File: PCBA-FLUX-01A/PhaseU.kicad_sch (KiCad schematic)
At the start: 60 parts, among them Q2 IPT015N10N5, Q3 IPT015N10N5, Q4 IPT015N10N5, Q5 IPT015N10N5, Q6 BC817, U2 INA240A2DR, U3 UCC27211AQDDARQ1, U4 TLV9001

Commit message: Changes were made
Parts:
- added C104: C, Capacitor_THT:C_Rect_L9.0mm_W6.4mm_P7.50mm_MKT, symbol Device:C
- added C95: 10nF, Capacitor_SMD:C_0603_1608Metric, symbol Device:C
- added R76, R77, R78, R79: 10R, Resistor_SMD:R_0805_2012Metric, symbol Device:R
- added R90: R, Resistor_SMD:R_1218_3246Metric, symbol Device:R
- R1, R17, R2: footprint Resistor_SMD:R_0805_2012Metric -> Resistor_SMD:R_0603_1608Metric
- R3: footprint Resistor_SMD:R_0805_2012Metric -> palmkiLib:R_0603_1608Metric
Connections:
- net GND: now also C104.2
- net phU_Shunt+: now also R76.1, R77.1; no longer U2.8 (IN+)
- net phU_Shunt-: now also R78.1, R79.1; no longer U2.1 (IN-)
- net at C37.2, C38.2, Q2.2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: now also R90.1
- new net: C95.1, R76.2, R77.2, U2.8 (IN+)
- new net: C95.2, R78.2, R79.2, U2.1 (IN-)
- new net: C104.1, R90.2
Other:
- moved on the sheet: C29, C30, C31, C32, C33, C34, C35, C36, C37, C38, D2, D3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

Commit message: Finished schematic?
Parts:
- removed C42, C44, C46, C49: 2.2uF, Capacitor_SMD:C_1210_3225Metric, symbol Device:C
- removed Q6: BC817, Package_TO_SOT_SMD:SOT-23, symbol Transistor_BJT:BC817
- removed R24: 2K2, Resistor_SMD:R_0603_1608Metric, symbol Device:R
- added C107, C108, C109, C110, C111: 1000uF, Capacitor_THT:CP_Radial_D18.0mm_P7.50mm, symbol Device:C_Polarized
- added C112, C113, C114, C115, C116: 10uF, Capacitor_SMD:C_1210_3225Metric, symbol Device:C
- added C117: 100nF, Capacitor_SMD:C_0805_2012Metric, symbol Device:C
- added Q18: BC860C, Package_TO_SOT_SMD:SOT-23, symbol Simulation_SPICE:PNP
- added R93: 18k, Resistor_SMD:R_0603_1608Metric, symbol Synapse:R
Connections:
- net +3.3VA: now also Q18.3 (E), R93.1
- net +VSYS: now also C107.1, C108.1, C109.1, C110.1, C111.1, C112.1, C113.1, C114.1, C115.1, C116.1, C117.1
- net GND: now also C107.2, C108.2, C109.2, C110.2, C111.2, C112.2, C113.2, C114.2, C115.2, C116.2, C117.2
- net at R21.2: now also Q18.2 (B)
- net at R22.2, R25.1, TH1.1: now also R93.2
- net at R22.1, R23.2: now also Q18.1 (C)
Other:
- note added: "Current Sense"
- note added: "DC-Link"
- note added: "Gate driver & bridge"
- note added: "Phase Temp"
- note added: "Phase Voltage"
- moved on the sheet: C104, C29, C30, C31, C32, C33, C34, C35, C36, C37, C38, C39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

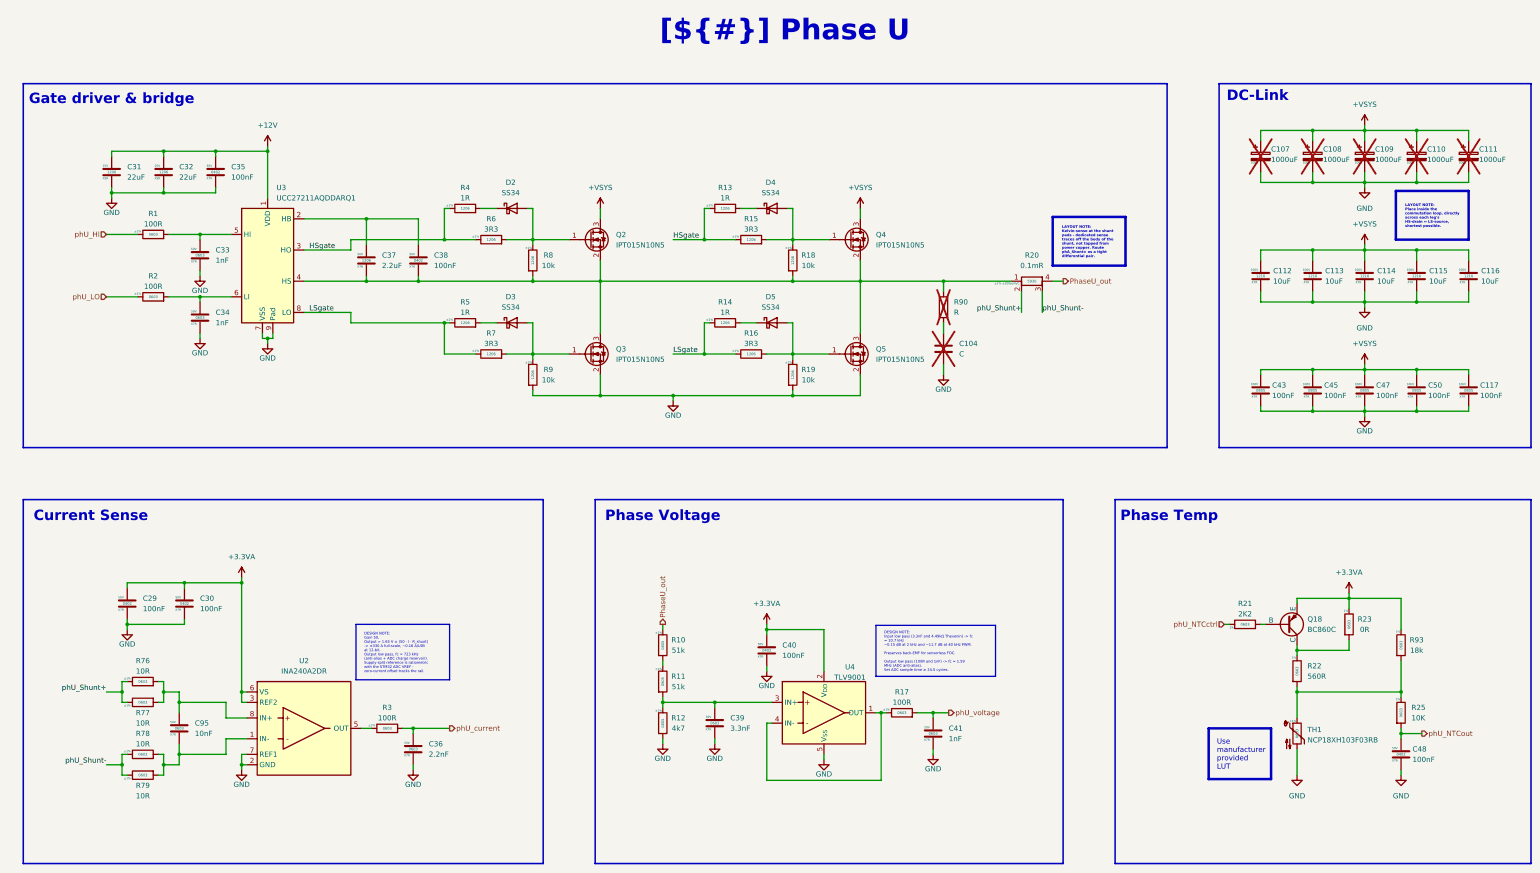
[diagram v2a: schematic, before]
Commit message: Moved the current and voltage sensing OpAmp's to Vector
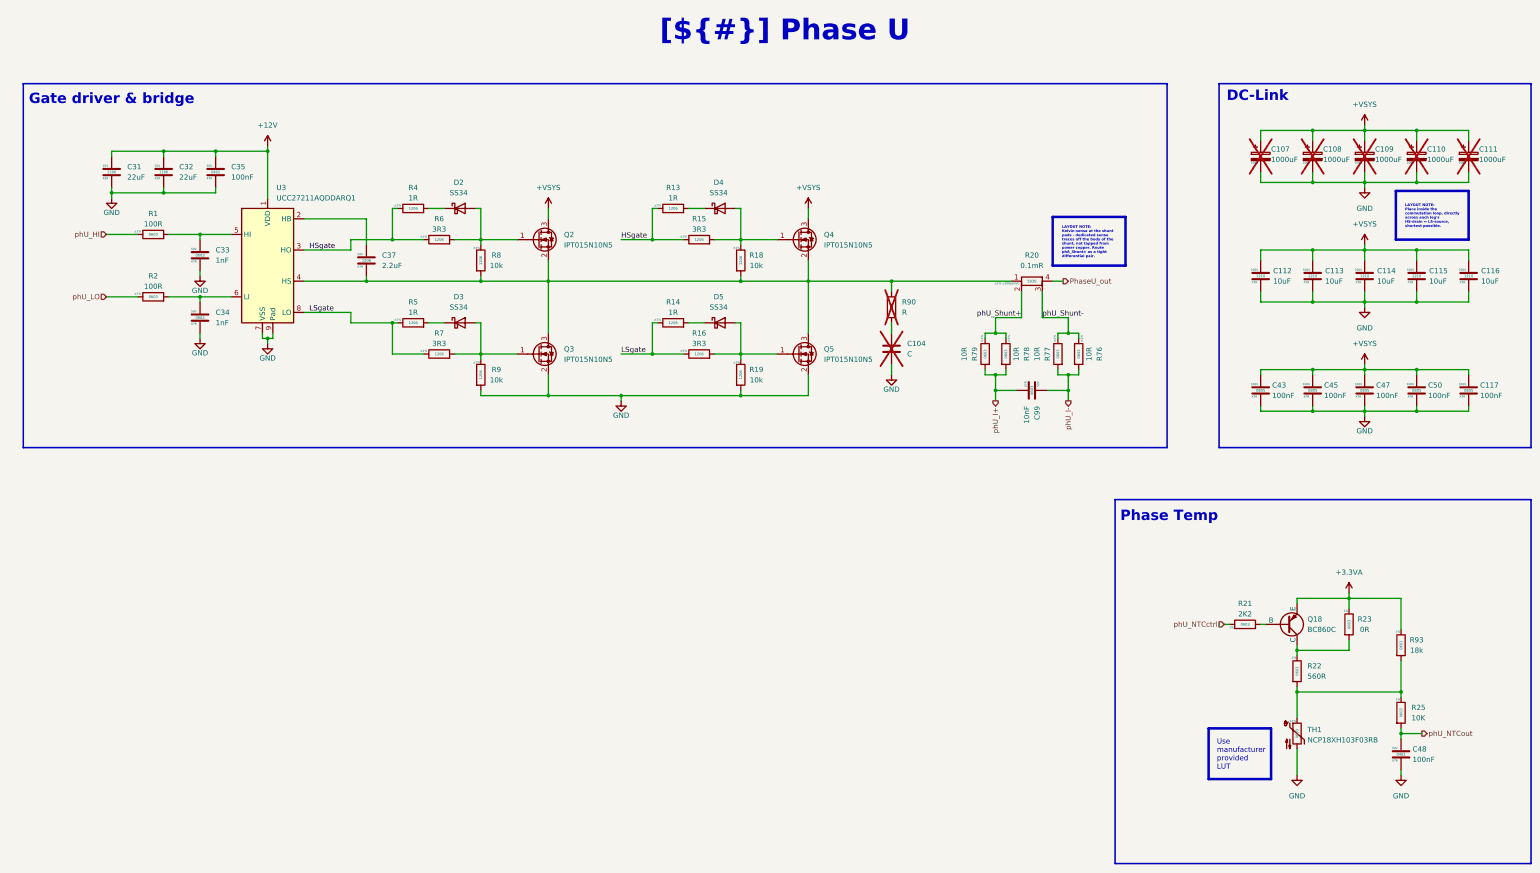
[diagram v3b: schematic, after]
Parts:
- removed C29, C30, C38, C40: 100nF, Capacitor_SMD:C_0402_1005Metric, symbol Device:C
- removed C36: 2.2nF, Capacitor_SMD:C_0603_1608Metric, symbol Device:C
- removed C39: 3.3nF, Capacitor_SMD:C_0603_1608Metric, symbol Device:C
- removed C41: 1nF, Capacitor_SMD:C_0603_1608Metric, symbol Device:C
- removed C95: 10nF, Capacitor_SMD:C_0603_1608Metric, symbol Device:C
- removed R10, R11: 51k, Resistor_SMD:R_0805_2012Metric, symbol Device:R
- removed R12: 4k7, Resistor_SMD:R_0805_2012Metric, symbol Device:R
- removed R17: 100R, Resistor_SMD:R_0603_1608Metric, symbol Device:R
- removed R3: 100R, palmkiLib:R_0603_1608Metric, symbol Device:R
- removed U2: INA240A2DR, Package_SO:SOIC-8_3.9x4.9mm_P1.27mm, symbol Bvrny's_library:INA240A2DR
- removed U4: TLV9001, Package_TO_SOT_SMD:SOT-23-5, symbol Bvrny's_library:TLV9001IDBVR
- added C99: 10nF, Capacitor_SMD:C_0603_1608Metric, symbol Device:C
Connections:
- net phU_Shunt+: now also R78.1, R79.1; no longer R76.1, R77.1
- net phU_Shunt-: now also R76.1, R77.1; no longer R78.1, R79.1
- net phU_I-: now reaches R76.2, R77.2
- net phU_I-: now also C99.1
- net phU_I+: now reaches R78.2, R79.2
- net phU_I+: now also C99.2
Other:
- note removed: "Current Sense"
- note removed: "Phase Voltage"
- moved on the sheet: C104, D2, D3, D4, D5, Q2, Q3, Q4, Q5, R13, R14, R15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
